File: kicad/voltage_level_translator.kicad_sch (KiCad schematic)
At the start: 18 parts, among them Q1 2N7002, Q2 2N7002, U1 TXS0108EPW, U2 TXS0108EPW, U3 TMUX1574PW, U4 TMUX1574PW

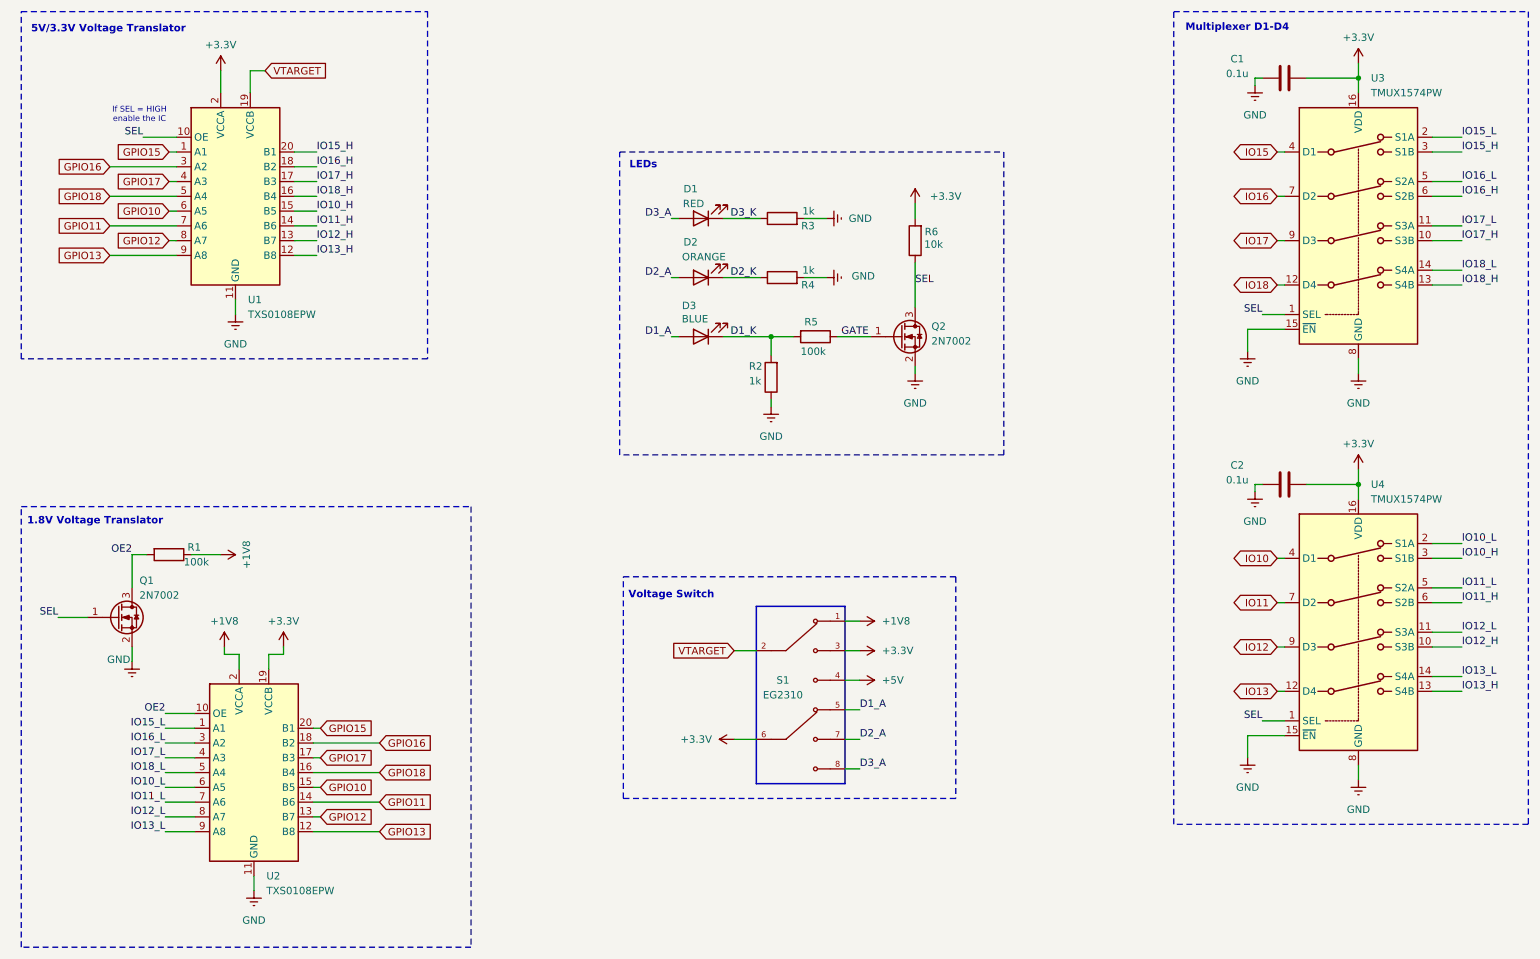
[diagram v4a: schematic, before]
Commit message: Updated PCB to include TXS disabling
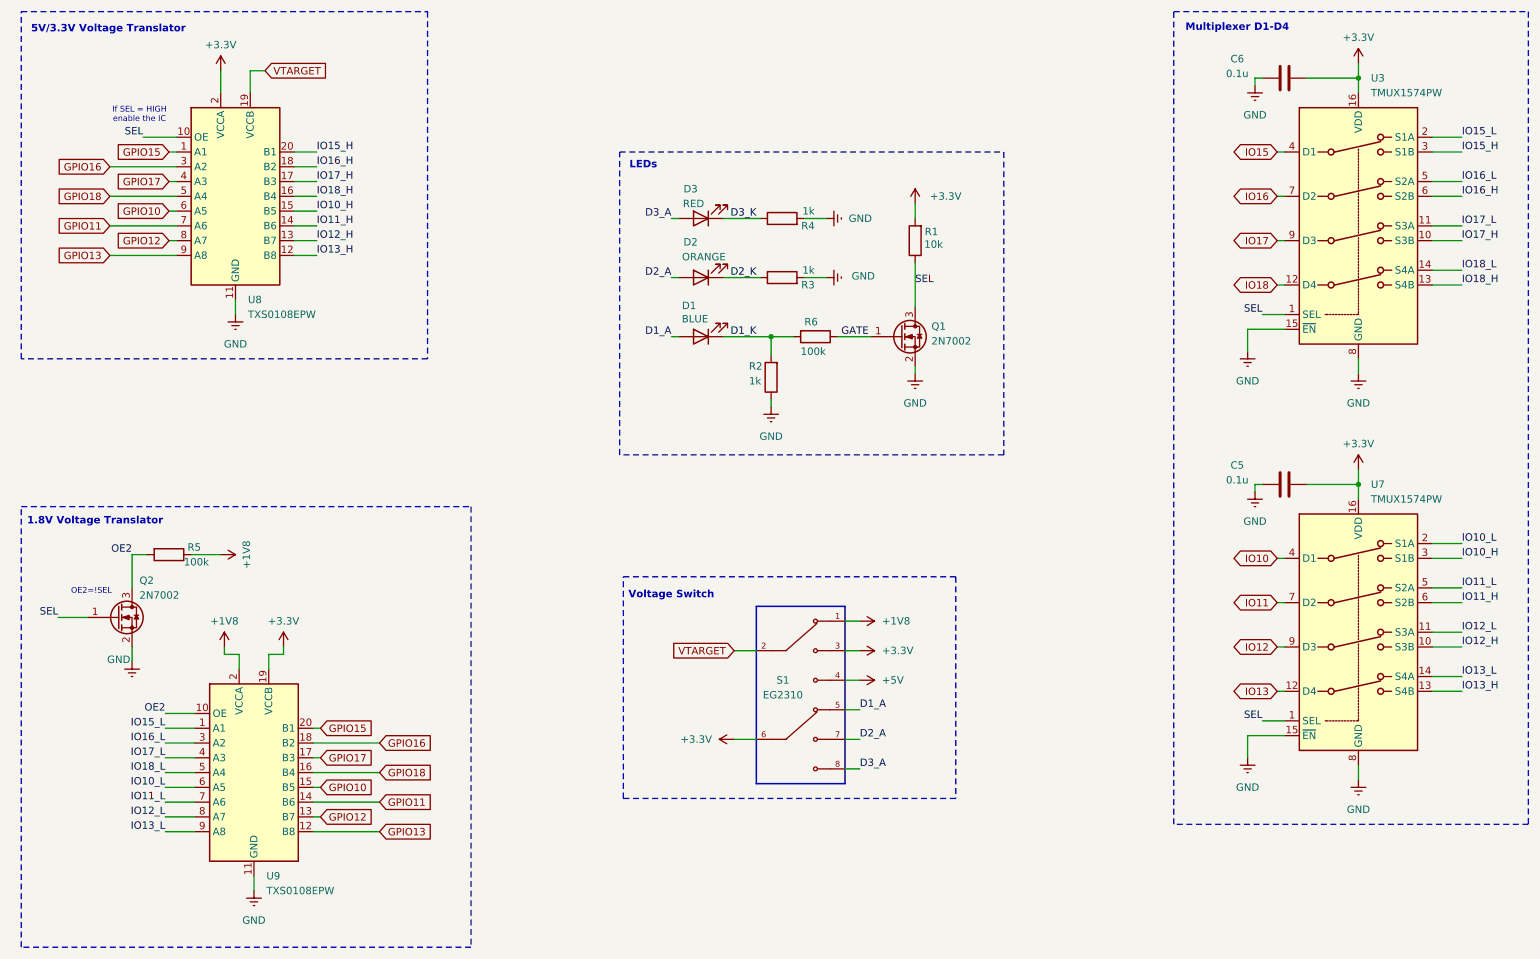
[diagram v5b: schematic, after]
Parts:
- renumbered C2 to C5, C1 to C6, D3 to D1, D1 to D3, Q2 to Q1, Q1 to Q2, R6 to R1, R4 to R3, R3 to R4, R1 to R5, R5 to R6, U4 to U7, U1 to U8, U2 to U9
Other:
- note added: "OE2=!SEL"
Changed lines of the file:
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@@
 		)
 	)
+	(text "OE2=!SEL"
+		(exclude_from_sim no)
+		(at 31.115 118.745 0)
+		(effects
+			(font
+				(size 1 1)
+				(thickness 0.1588)
+				(color 132 132 0 1)
+			)
+		)
+	)
 	(text "5V/3.3V Voltage Translator"
 		(exclude_from_sim no)
@@
 				)
 				(justify right)
-				(hide yes)
 			)
 		)
@@
 				)
 				(justify left)
-				(hide yes)
 			)
 		)
@@
 				)
 				(justify right)
-				(hide yes)
 			)
 		)
@@
 				)
 				(justify left)
-				(hide yes)
 			)
 		)
@@
 				)
 				(justify right)
-				(hide yes)
 			)
 		)
@@
 				)
 				(justify right)
-				(hide yes)
 			)
 		)
@@
 				)
 				(justify right)
-				(hide yes)
 			)
 		)
@@
 				)
 				(justify left)
-				(hide yes)
 			)
 		)
@@
 				)
 				(justify right)
-				(hide yes)
 			)
 		)
@@
 				)
 				(justify right)
-				(hide yes)
 			)
 		)
@@
 				)
 				(justify right)
-				(hide yes)
 			)
 		)
@@
 				)
 				(justify left)
-				(hide yes)
 			)
 		)
@@
 				)
 				(justify right)
-				(hide yes)
 			)
 		)
@@
 				)
 				(justify right)
-				(hide yes)
 			)
 		)
@@
 				)
 				(justify left)
-				(hide yes)
 			)
 		)
@@
 				)
 				(justify right)
-				(hide yes)
 			)
 		)
@@
 				)
 				(justify left)
-				(hide yes)
 			)
 		)
@@
 				)
 				(justify right)
-				(hide yes)
 			)
 		)
@@
 				)
 				(justify left)
-				(hide yes)
 			)
 		)
@@
 				)
 				(justify right)
-				(hide yes)
 			)
 		)
@@
 				)
 				(justify right)
-				(hide yes)
 			)
 		)
@@
 				)
 				(justify right)
-				(hide yes)
 			)
 		)
@@
 				)
 				(justify right)
-				(hide yes)
 			)
 		)
@@
 				)
 				(justify left)
-				(hide yes)
 			)
 		)
@@
 				)
 				(justify right)
-				(hide yes)
 			)
 		)
@@
 				)
 				(justify left)
-				(hide yes)
 			)
 		)
@@
 		(dnp no)
 		(fields_autoplaced yes)
-		(property "Reference" "#PWR0105"
+		(property "Reference" "#PWR048"
 			(at 248.92 87.63 0)
 			(effects
@@
 		(dnp no)
 		(fields_autoplaced yes)
-		(property "Reference" "#PWR0108"
+		(property "Reference" "#PWR035"
 			(at 229.87 153.67 0)
 			(effects
@@
 		(dnp no)
 		(fields_autoplaced yes)
-		(property "Reference" "#PWR0118"
+		(property "Reference" "#PWR037"
 			(at 64.135 132.08 0)
 			(effects
@@
 		(dnp no)
 		(fields_autoplaced yes)
-		(property "Reference" "#PWR0116"
+		(property "Reference" "#PWR020"
 			(at 159.385 133.985 0)
 			(effects
@@
 		(dnp no)
 		(fields_autoplaced yes)
-		(property "Reference" "#PWR0115"
+		(property "Reference" "#PWR022"
 			(at 159.385 123.825 0)
 			(effects
@@
 		(dnp no)
 		(fields_autoplaced yes)
-		(property "Reference" "U1"
+		(property "Reference" "U8"
 			(at 58.0233 68.58 0)
 			(effects
@@
 		(dnp no)
 		(fields_autoplaced yes)
-		(property "Reference" "#PWR0121"
+		(property "Reference" "#PWR01"
 			(at 53.34 33.02 0)
 			(effects
@@
 		(on_board yes)
 		(dnp no)
-		(property "Reference" "#PWR0109"
+		(property "Reference" "#PWR041"
 			(at 163.83 64.77 0)
 			(effects
@@
 		(on_board yes)
 		(dnp no)
-		(property "Reference" "#PWR0122"
+		(property "Reference" "#PWR012"
 			(at 38.1 137.16 0)
 			(effects
@@
 		(dnp no)
 		(fields_autoplaced yes)
-		(property "Reference" "#PWR0110"
+		(property "Reference" "#PWR032"
 			(at 163.83 54.61 0)
 			(effects
@@
 		(on_board yes)
 		(dnp no)
-		(property "Reference" "R4"
+		(property "Reference" "R3"
 			(at 155.448 66.04 90)
 			(effects
@@
 		(dnp no)
 		(fields_autoplaced yes)
-		(property "Reference" "U2"
+		(property "Reference" "U9"
 			(at 61.1983 167.64 0)
 			(effects
@@
 		(dnp no)
 		(fields_autoplaced yes)
-		(property "Reference" "#PWR0107"
+		(property "Reference" "#PWR049"
 			(at 248.92 157.48 0)
 			(effects
@@
 		(dnp no)
 		(fields_autoplaced yes)
-		(property "Reference" "#PWR0120"
+		(property "Reference" "#PWR019"
 			(at 55.88 77.47 0)
 			(effects
@@
 		(dnp no)
 		(fields_autoplaced yes)
-		(property "Reference" "#PWR0112"
+		(property "Reference" "#PWR042"
 			(at 147.955 93.345 0)
 			(effects
@@
 		(dnp no)
 		(fields_autoplaced yes)
-		(property "Reference" "#PWR0103"
+		(property "Reference" "#PWR033"
 			(at 231.14 107.95 0)
 			(effects
@@
 		(dnp no)
 		(fields_autoplaced yes)
-		(property "Reference" "#PWR0101"
+		(property "Reference" "#PWR034"
 			(at 231.14 38.1 0)
 			(effects
@@
 		(dnp no)
 		(fields_autoplaced yes)
-		(property "Reference" "#PWR0104"
+		(property "Reference" "#PWR036"
 			(at 229.87 83.82 0)
 			(effects
@@
 		(dnp no)
 		(fields_autoplaced yes)
-		(property "Reference" "#PWR0106"
+		(property "Reference" "#PWR038"
 			(at 248.92 101.6 0)
 			(effects
@@
 		(dnp no)
 		(fields_autoplaced yes)
-		(property "Reference" "#PWR0111"
+		(property "Reference" "#PWR061"
 			(at 172.72 87.63 0)
 			(effects
@@
 		(on_board yes)
 		(dnp no)
-		(property "Reference" "R6"
+		(property "Reference" "R1"
 			(at 175.514 56.896 0)
 			(effects
@@
 		(dnp no)
 		(fields_autoplaced yes)
-		(property "Reference" "U4"
+		(property "Reference" "U7"
 			(at 251.0633 100.33 0)
 			(effects
@@
 		(dnp no)
 		(fields_autoplaced yes)
-		(property "Reference" "#PWR0119"
+		(property "Reference" "#PWR039"
 			(at 59.055 176.53 0)
 			(effects
@@
 		(on_board yes)
 		(dnp no)
-		(property "Reference" "R5"
+		(property "Reference" "R6"
 			(at 153.67 72.39 90)
 			(effects
@@
 		(dnp no)
 		(fields_autoplaced yes)
-		(property "Reference" "#PWR0114"
+		(property "Reference" "#PWR055"
 			(at 145.415 144.145 0)
 			(effects
@@
 		(on_board yes)
 		(dnp no)
-		(property "Reference" "#PWR0123"
+		(property "Reference" "#PWR024"
 			(at 53.975 132.08 0)
 			(effects
@@
 		(on_board yes)
 		(dnp no)
-		(property "Reference" "R1"
+		(property "Reference" "R5"
 			(at 47.625 111.125 90)
 			(effects
@@
 		(dnp no)
 		(fields_autoplaced yes)
-		(property "Reference" "#PWR0102"
+		(property "Reference" "#PWR040"
 			(at 248.92 31.75 0)
 			(effects
@@
 		(on_board yes)
 		(dnp no)
-		(property "Reference" "Q2"
+		(property "Reference" "Q1"
 			(at 175.514 73.152 0)
 			(effects
@@
 		(dnp no)
 		(fields_autoplaced yes)
-		(property "Reference" "#PWR0113"
+		(property "Reference" "#PWR060"
 			(at 172.72 55.88 0)
 			(effects
@@
 		(on_board yes)
 		(dnp no)
-		(property "Reference" "D1"
+		(property "Reference" "D3"
 			(at 134.112 49.53 0)
 			(effects
@@
 		(on_board yes)
 		(dnp no)
-		(property "Reference" "C1"
+		(property "Reference" "C6"
 			(at 228.092 27.178 90)
 			(effects
@@
 		(on_board yes)
 		(dnp no)
-		(property "Reference" "D3"
+		(property "Reference" "D1"
 			(at 133.858 69.596 0)
 			(effects
@@
 		(on_board yes)
 		(dnp no)
-		(property "Reference" "R3"
+		(property "Reference" "R4"
 			(at 155.448 55.88 90)
 			(effects
@@
 		(on_board yes)
 		(dnp no)
-		(property "Reference" "C2"
+		(property "Reference" "C5"
 			(at 228.092 97.028 90)
 			(effects
@@
 		(on_board yes)
 		(dnp no)
-		(property "Reference" "Q1"
+		(property "Reference" "Q2"
 			(at 39.37 116.84 0)
 			(effects
@@
 		(on_board yes)
 		(dnp no)
-		(property "Reference" "#PWR0124"
+		(property "Reference" "#PWR023"
 			(at 49.53 112.395 0)
 			(effects
@@
 		(dnp no)
 		(fields_autoplaced yes)
-		(property "Reference" "#PWR0117"
+		(property "Reference" "#PWR021"
 			(at 159.385 128.905 0)
 			(effects

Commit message: Reduced Logic circuit
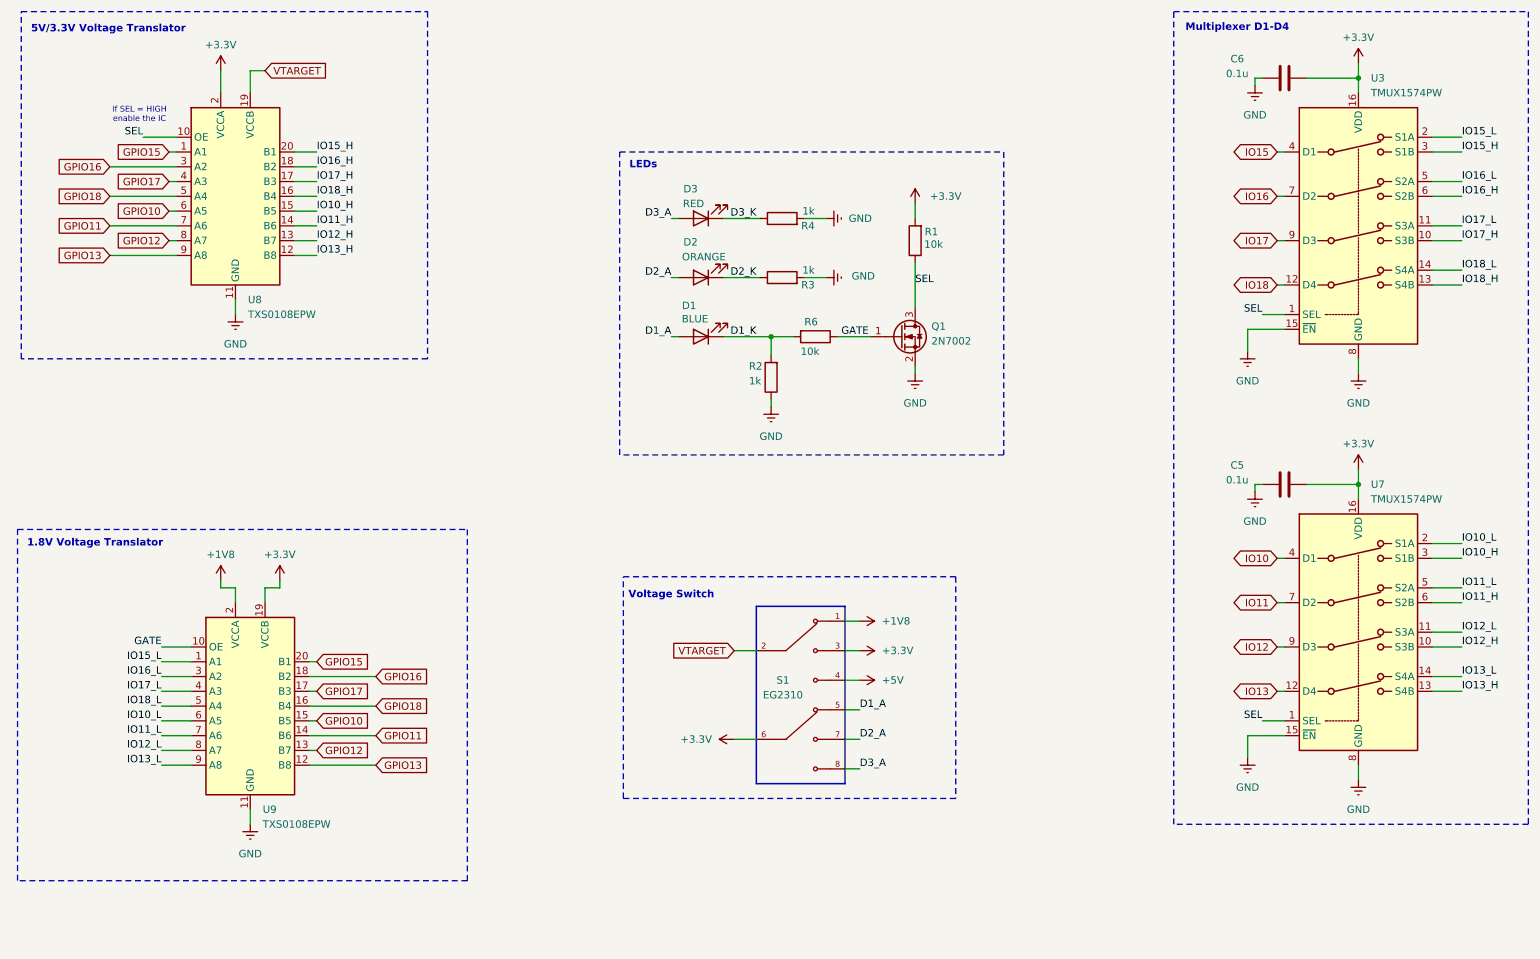
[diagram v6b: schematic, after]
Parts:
- removed Q2: 2N7002, Package_TO_SOT_SMD:SOT-23, symbol Transistor_FET:2N7002
- removed R5: 100k, Resistor_SMD:R_0805_2012Metric, symbol Device:R
- R6: value 100k -> 10k
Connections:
- net OE2 is gone; now on net GATE: U9.10 (OE)
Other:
- note removed: "OE2=!SEL"
- moved on the sheet: U9

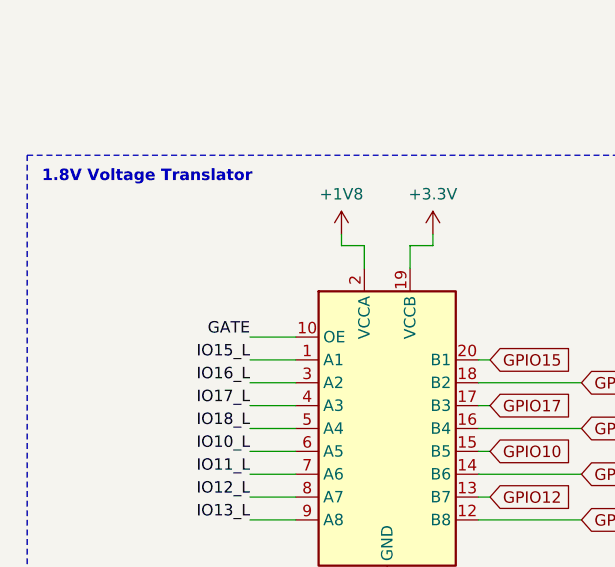
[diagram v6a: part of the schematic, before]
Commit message: Changed track widths  to 1.524mm
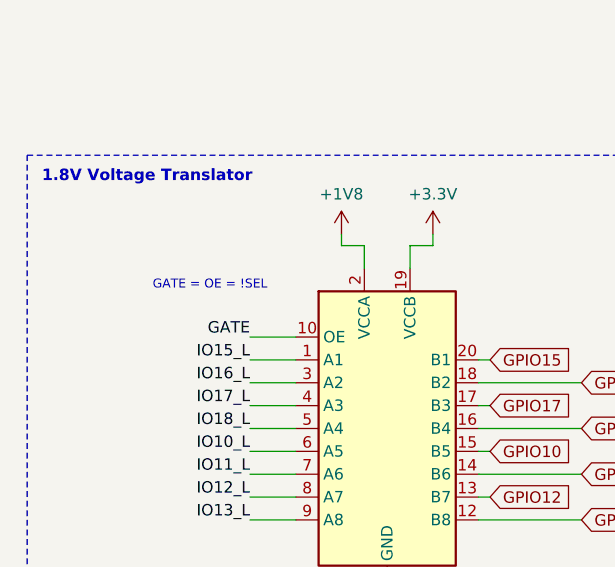
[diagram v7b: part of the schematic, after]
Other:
- note added: "GATE = OE = !SEL"
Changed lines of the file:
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@@
+		)
+	)
+	(text "GATE = OE = !SEL"
+		(exclude_from_sim no)
+		(at 38.735 122.555 0)
+		(effects
+			(font
+				(size 1 1)
+				(thickness 0.1588)
+				(color 132 132 0 1)
+			)
 		)
 	)

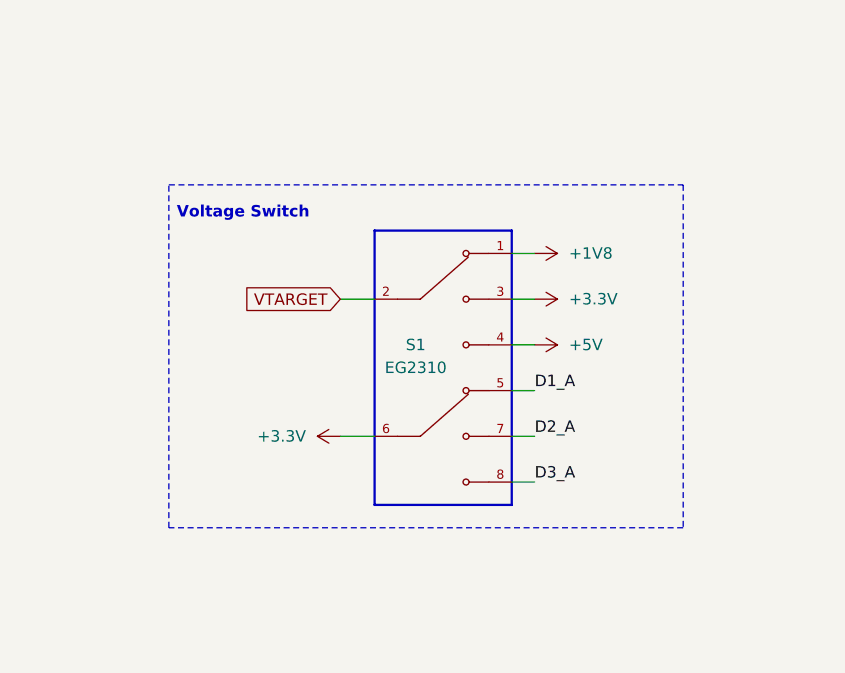
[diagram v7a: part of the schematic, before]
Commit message: Changed DP3T switch
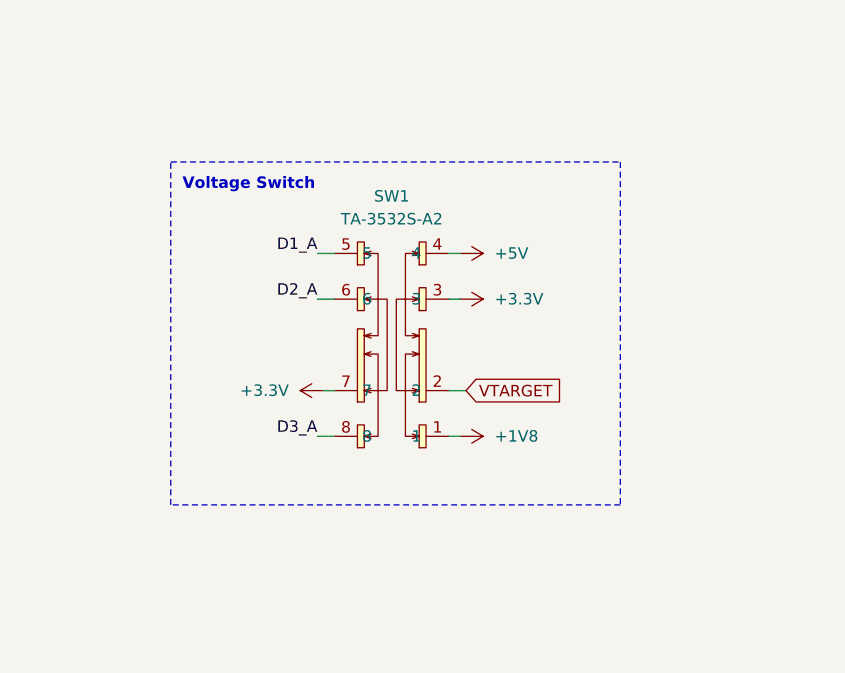
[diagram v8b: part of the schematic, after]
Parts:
- removed S1: EG2310, EG2310:SW_EG2310, symbol EG2310:EG2310
- added SW1: TA-3532S-A2, TA-3532S-A2:SW-SMD_8P-L13.0-W3.5-P2.00, symbol easyeda2kicad:TA-3532S-A2
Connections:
- net +1V8: now also SW1.1
- net +3.3V: now also SW1.3, SW1.7
- net +5V: now also SW1.4
- net D1_A: now also SW1.5
- net D2_A: now also SW1.6
- net D3_A: now also SW1.8
- net VTARGET: now also SW1.2
